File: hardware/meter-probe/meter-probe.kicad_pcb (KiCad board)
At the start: 4 copper layers, 40 x 74 mm, 40 parts, among them J1 Cable, J2 Cable, SW1 Sensor Button, U1 TSL2585, U2 M24C02-D, U3 PCA9527, U4 TC1301A-APA, U5 USBLC6-2SC6

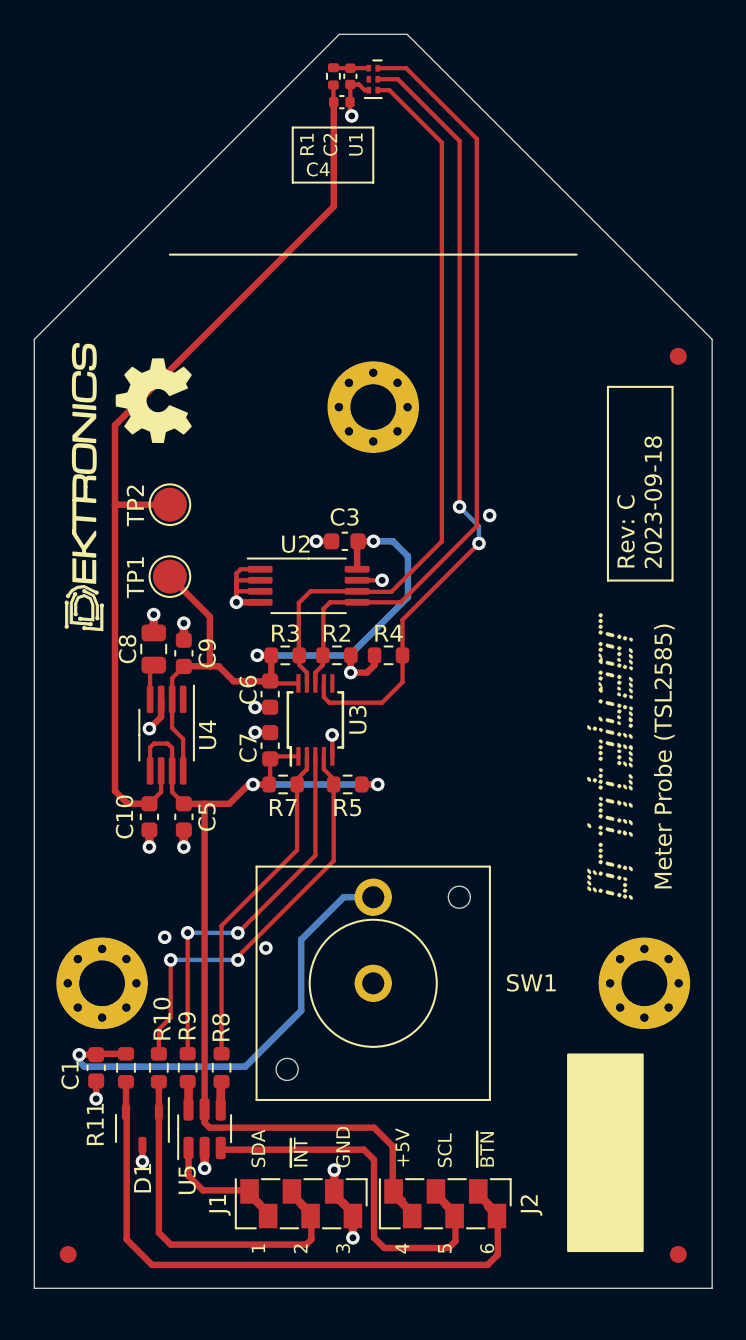
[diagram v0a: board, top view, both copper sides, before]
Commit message: Update meter probe with a variety of changes based on testing and eval
- Add a TCA9801 I2C buffer to remove the static offset induced by the
  PCA9527 and provide a clean 1.8V I2C signal to the sensor.
  While the board does work fine without this, the 0.5V static offset
  from the PCA9527 is too close for comfort to the sensor's 0.54V low
  level. So this is a proactive change to reduce potential issues later.
- Add a small series resistor to the push button, to limit the current
  across the debounce capacitor when the button is pressed.
- Add a series of test points at the board edge, so a pogo pin test clip
  can be used more easily to verify board operation prior to attachment
  of the interfae cable.
- Increase board length by 1mm to accomodate the test points.
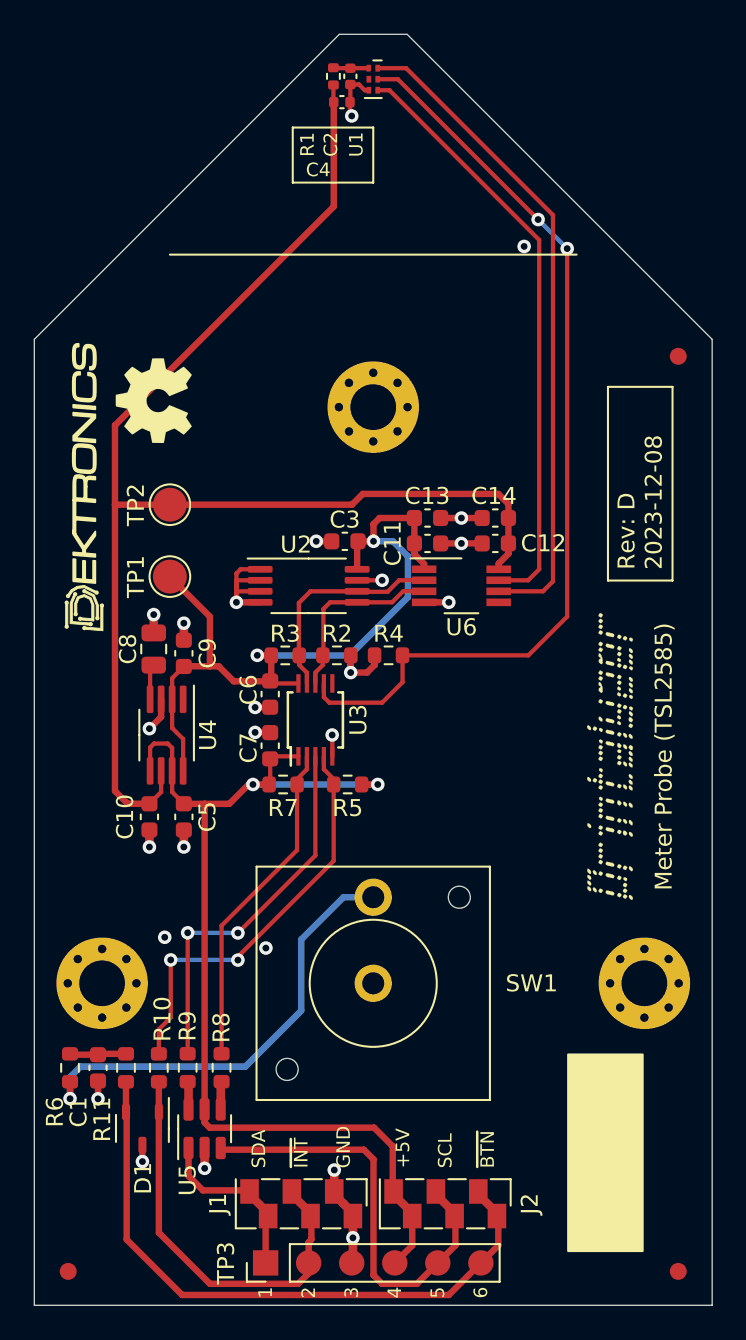
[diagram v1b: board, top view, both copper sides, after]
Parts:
- added C11: 0.1uF, Capacitor_SMD:C_0603_1608Metric, F.Cu at (123.2, 90.0)
- added C12: 0.1uF, Capacitor_SMD:C_0603_1608Metric, F.Cu at (127.2, 90.0)
- added C13: 1uF, Capacitor_SMD:C_0603_1608Metric, F.Cu at (123.2, 88.5)
- added C14: 1uF, Capacitor_SMD:C_0603_1608Metric, F.Cu at (127.2, 88.5)
- added R6: 220R, Resistor_SMD:R_0603_1608Metric, F.Cu at (102.1, 121.0)
- added TP3: Test, lib_fp:TestPoint_1x06_P2.54mm, F.Cu at (113.7, 132.5)
- added U6: TCA9801, Package_SO:VSSOP-8_3.0x3.0mm_P0.65mm, F.Cu at (125.2, 92.5)
- moved FID1 1.00 mm to (102.0, 133.0)
- moved FID2 1.00 mm to (138.0, 133.0)
- moved C1 0.11 mm to (103.8, 121.0)
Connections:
- R2 pad 2: /SENSOR_SDA -> /3V3_SDA
- R3 pad 2: /SENSOR_SCL -> /3V3_SCL
- SW1 pad 2: /PROBE_BTN -> Net-(R6-Pad1)
- U2 pad 5: /SENSOR_SDA -> /3V3_SDA
- U2 pad 6: /SENSOR_SCL -> /3V3_SCL
- U3 pad 8: /SENSOR_SDA -> /3V3_SDA
- U3 pad 9: /SENSOR_SCL -> /3V3_SCL
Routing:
- net Net-(R6-Pad1): track 0.00 -> 27.0 mm, vias 0 -> 1
- net +1V8: track 54.8 -> 79.4 mm
- net /PROBE_BTN: track 27.2 -> 3.20 mm, vias 1 -> 0
- net /3V3_SCL: track 0.00 -> 12.9 mm
- net /3V3_SDA: track 0.00 -> 11.0 mm
- net /SENSOR_INT: track 46.7 -> 55.4 mm
- net /SENSOR_SCL: track 43.5 -> 35.3 mm
- net GND: track 31.6 -> 39.4 mm, vias 20 -> 23
- net /SENSOR_SDA: track 46.1 -> 39.0 mm
- net +3.3V: track 44.1 -> 50.9 mm
- net +5V: track 57.4 -> 59.7 mm
- net /PROBE_CONN_SCL: track 21.5 -> 23.7 mm
- net /PROBE_CONN_INT: track 20.8 -> 22.8 mm
- net /PROBE_CONN_SDA: track 6.53 -> 8.14 mm
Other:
- board size 40 x 74 mm -> 40 x 75 mm

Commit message: Initial layout for USB meter probe design
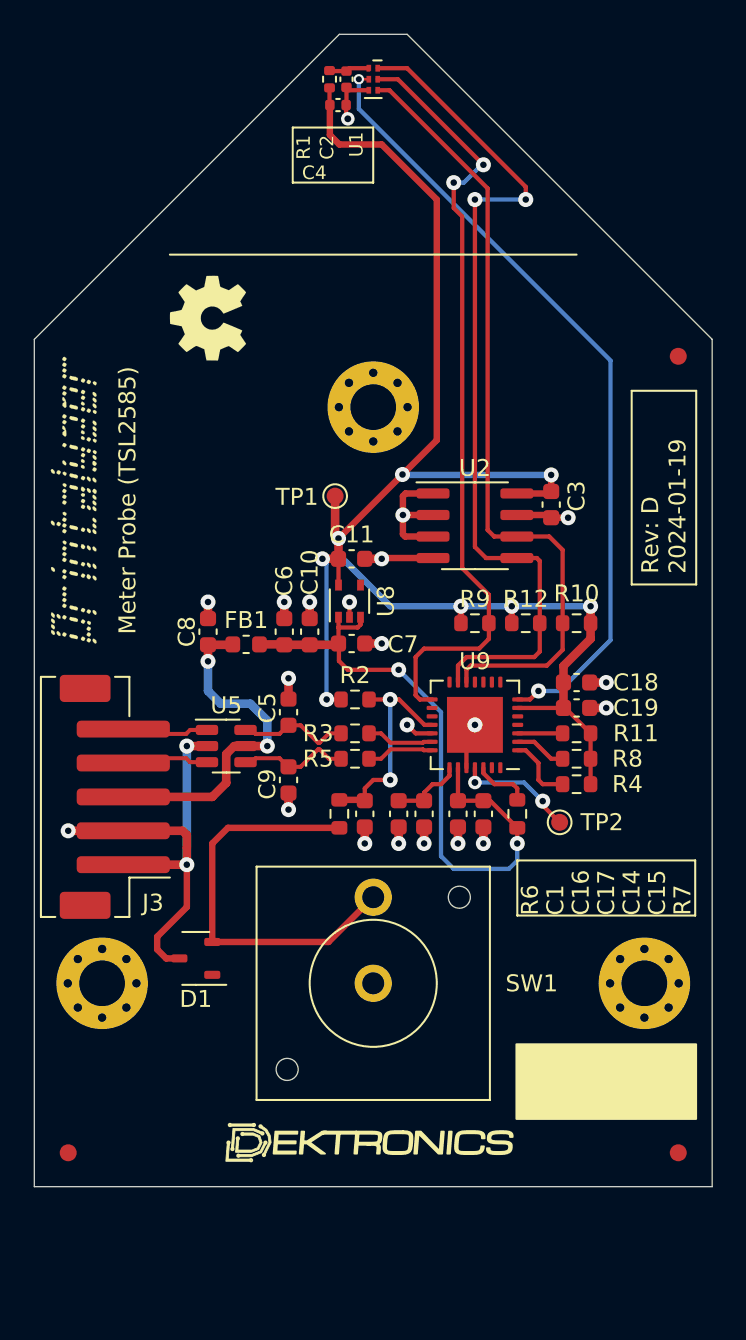
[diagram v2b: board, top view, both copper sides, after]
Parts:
- removed C12: 0.1uF, Capacitor_SMD:C_0603_1608Metric
- removed C13: 1uF, Capacitor_SMD:C_0603_1608Metric
- removed J1, J2: Cable, lib_fp:AVX_IDC-009175-003-001
- removed TP3: Test, lib_fp:TestPoint_1x06_P2.54mm
- removed U3: PCA9527, Package_SO:TSSOP-10_3x3mm_P0.5mm
- removed U4: TC1301A-APA, Package_SO:MSOP-8_3x3mm_P0.65mm
- removed U6: TCA9801, Package_SO:VSSOP-8_3.0x3.0mm_P0.65mm
- added C15: 0.1uF, Capacitor_SMD:C_0603_1608Metric, F.Cu at (126.5, 106.0)
- added C16: 4.7uF, Capacitor_SMD:C_0603_1608Metric, F.Cu at (121.5, 106.0)
- added C17: 0.1uF, Capacitor_SMD:C_0603_1608Metric, F.Cu at (123.0, 106.0)
- added C18: 4.7uF, Capacitor_SMD:C_0603_1608Metric, F.Cu at (132.0, 98.2)
- added C19: 0.1uF, Capacitor_SMD:C_0603_1608Metric, F.Cu at (132.0, 99.8)
- added FB1: 600R@100MHz, Inductor_SMD:L_0603_1608Metric, F.Cu at (112.5, 96.0)
- added J3: Cable, Connector_JST:JST_PH_B5B-PH-SM4-TB_1x05-1MP_P2.00mm_Vertical, F.Cu at (104.8, 105.0)
- added NT1: NetTie_2, NetTie:NetTie-2_SMD_Pad0.5mm, F.Cu at (109.0, 108.5)
- added R12: 1K, Resistor_SMD:R_0603_1608Metric, F.Cu at (129.0, 94.8)
- added U8: MIC5365-1.8YC5, Package_TO_SOT_SMD:SOT-353_SC-70-5, F.Cu at (118.6, 93.5)
- added U9: FT260Q, lib_fp:FTDI_WQFN-28-1EP_5x5mm_P0.5mm_EP3.3x3.3mm, F.Cu at (126.0, 100.8)
- C10: value 1uF -> 0.1uF
- C11, C7: value 0.1uF -> 1uF
- C14: value 1uF -> 4.7uF
- C5, C9: value 1uF -> 47pF
- C6: value 0.1uF -> 4.7uF
- C8: footprint Capacitor_SMD:C_0805_2012Metric -> Capacitor_SMD:C_0603_1608Metric
- R10: value 33R -> 1K
- R11: value 220R -> 10K
- R2: value 2K -> 10K
- R3: value 2K -> 33R
- R5: value 10K -> 33R
- R7: value 47K -> 5.1k
- R8, R9: value 33R -> 10K
- TP1: value 3.3V -> TestPoint; footprint TestPoint:TestPoint_Pad_D2.0mm -> TestPoint:TestPoint_Pad_D1.0mm
- TP2: value 1.8V -> TestPoint; footprint TestPoint:TestPoint_Pad_D2.0mm -> TestPoint:TestPoint_Pad_D1.0mm
- U2: value M24C02-D -> CAT24C08; footprint Package_SO:TSSOP-8_4.4x3mm_P0.65mm -> Package_SO:SOIC-8_3.9x4.9mm_P1.27mm
- moved LOGO 42.4 mm to (120.0, 125.2), turned to 0 degrees
- moved R10 36.0 mm to (132.0, 94.8), turned to 180 degrees
- moved G*** 35.1 mm to (102.3, 87.5)
- moved R11 33.1 mm to (132.0, 101.2), turned to 180 degrees
- moved R9 31.2 mm to (126.0, 94.8), turned to 0 degrees
- moved TP2 29.7 mm to (131.0, 106.5), turned to 180 degrees
- moved R8 27.8 mm to (132.0, 102.8), turned to 180 degrees
- moved U5 22.6 mm to (111.3, 102.0), turned to 0 degrees
- moved R6 21.8 mm to (118.0, 106.0)
- moved C1 21.7 mm to (119.5, 106.0)
- moved C14 17.6 mm to (125.0, 106.0), turned to -90 degrees
- moved C10 14.5 mm to (116.2, 95.2)
- moved R7 13.9 mm to (128.5, 106.0), turned to -90 degrees
- moved R4 13.5 mm to (132.0, 104.2), turned to 180 degrees
- moved C3 12.4 mm to (130.5, 87.8), turned to 90 degrees
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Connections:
- C10 pad 1: GND -> +5V
- C10 pad 2: +1V8 -> GND
- C11 pad 1: +3.3V -> +1V8
- C14 pad 1: +1V8 -> +5V
- C3 pad 2: +3.3V -> +1V8
- C5 pad 1: GND -> /USB_DI+
- C5 pad 2: +5V -> GND
- C6 pad 1: +3.3V -> +5V
- C7 pad 1: GND -> +5V
- C7 pad 2: +5V -> GND
- C8 pad 2: Net-(U4-BYPASS) -> VBUS
- C9 pad 1: GND -> /USB_DI-
- C9 pad 2: +3.3V -> GND
- D1 pad 1: /PROBE_CONN_INT -> unconnected-(D1-K-Pad1)
- D1 pad 2: /PROBE_CONN_BTN -> Net-(D1-K-Pad2)
- D1 pad 3: GND -> Earth
- R10 pad 1: /PROBE_INT -> +1V8
- R10 pad 2: /PROBE_CONN_INT -> /I2C_SCL
- R11 pad 1: /PROBE_BTN -> +1V8
- R11 pad 2: /PROBE_CONN_BTN -> Net-(U9-~{RESET})
- R2 pad 1: +3.3V -> +1V8
- R2 pad 2: /3V3_SDA -> /PROBE_BTN
- R3 pad 1: +3.3V -> /USB_D+
- R3 pad 2: /3V3_SCL -> /USB_DI+
- R4 pad 1: +3.3V -> +1V8
- R4 pad 2: /SENSOR_INT -> Net-(U9-DEBUGGER)
- R5 pad 1: +5V -> /USB_D-
- R5 pad 2: /PROBE_INT -> /USB_DI-
- R6 pad 1: Net-(R6-Pad1) -> Net-(D1-K-Pad2)
- R7 pad 1: +5V -> Net-(U9-VBUS_DET)
- R7 pad 2: /PROBE_SCL -> +5V
- R8 pad 1: /PROBE_SCL -> +1V8
- R8 pad 2: Net-(R8-Pad2) -> Net-(U9-~{STEST_RST})
- R9 pad 1: /PROBE_SDA -> +1V8
- R9 pad 2: Net-(R9-Pad2) -> /TSL_INT
- SW1 pad 2: Net-(R6-Pad1) -> Net-(D1-K-Pad2)
- TP1 pad 1: +3.3V -> +1V8
- TP2 pad 1: +1V8 -> Net-(U9-FSOURCE)
- U1 pad 2: unconnected-(U1-VSYNC/GPIO-Pad2) -> /TSL_VSYNC
- U1 pad 4: /SENSOR_SCL -> /I2C_SCL
- U1 pad 5: /SENSOR_INT -> /TSL_INT
- U1 pad 6: /SENSOR_SDA -> /I2C_SDA
- U2 pad 5: /3V3_SDA -> /I2C_SDA
- U2 pad 6: /3V3_SCL -> /I2C_SCL
- U2 pad 8: +3.3V -> +1V8
- U5 pad 1: /PROBE_CONN_SDA -> /USB_CONN_D+
- U5 pad 2: GND -> Earth
- U5 pad 3: /PROBE_CONN_SCL -> /USB_CONN_D-
- U5 pad 4: Net-(R8-Pad2) -> /USB_DI-
- U5 pad 5: +5V -> VBUS
- U5 pad 6: Net-(R9-Pad2) -> /USB_DI+
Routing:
- net /SENSOR_INT: track 55.4 -> 0.00 mm, vias 2 -> 0
- net /I2C_SDA: track 0.00 -> 51.5 mm, vias 0 -> 2
- net +3.3V: track 50.9 -> 0.00 mm, vias 3 -> 0
- net /TSL_VSYNC: track 0.00 -> 46.8 mm, vias 0 -> 2
- net /I2C_SCL: track 0.00 -> 46.7 mm
- net /TSL_INT: track 0.00 -> 46.4 mm, vias 0 -> 2
- net /SENSOR_SDA: track 39.0 -> 0.00 mm
- net /PROBE_CONN_BTN: track 35.7 -> 0.00 mm
- net /SENSOR_SCL: track 35.3 -> 0.00 mm
- net Net-(R6-Pad1): track 27.0 -> 0.00 mm, vias 1 -> 0
- net Net-(D1-K-Pad2): track 0.00 -> 24.3 mm
- net /PROBE_INT: track 24.0 -> 0.00 mm, vias 2 -> 0
- net /PROBE_CONN_SCL: track 23.7 -> 0.00 mm
- net /PROBE_CONN_INT: track 22.8 -> 0.00 mm
- net /PROBE_SDA: track 22.4 -> 0.00 mm, vias 2 -> 0
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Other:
- board size 40 x 75 mm -> 40 x 68 mm
- board text removed: "+5V"
- board text removed: "1"
- board text removed: "2"
- board text removed: "3"
- board text removed: "4"
- board text removed: "5"
- board text removed: "6"
- board text removed: "GND"
- board text removed: "SCL"
- board text removed: "SDA"
- board text removed: "~{BTN}"
- board text removed: "~{INT}"

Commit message: Clean up reference designators
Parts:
- renumbered C2 to C1, C14 to C10, C15 to C11, C16 to C12, C17 to C13, C18 to C14, C19 to C15, C3 to C16, C1 to C17, C4 to C2, C5 to C3, C9 to C4, C8 to C5, C10 to C7, C7 to C8, C11 to C9, J3 to J1, R7 to R10, R2 to R11, R6 to R12, R3 to R2, R5 to R3, R10 to R4, R12 to R5, R9 to R6, R11 to R7, R4 to R9, U5 to U2, U8 to U3, U9 to U4, U2 to U5

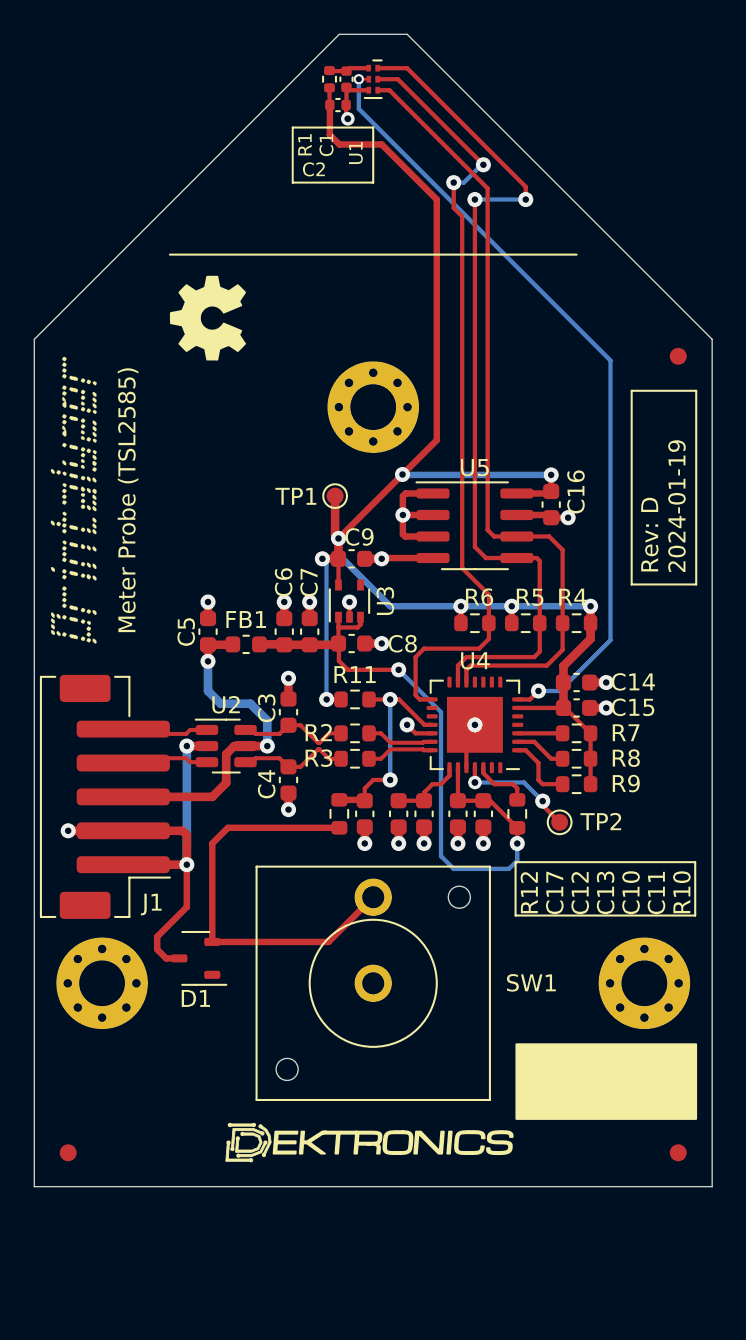
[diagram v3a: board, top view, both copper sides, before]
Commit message: Nudge some positions around
Moved the USB input components and routing to more closely match how the
evaluation board does it, only doing proper differential trace spacing
on the connector and FT260 endpoints.
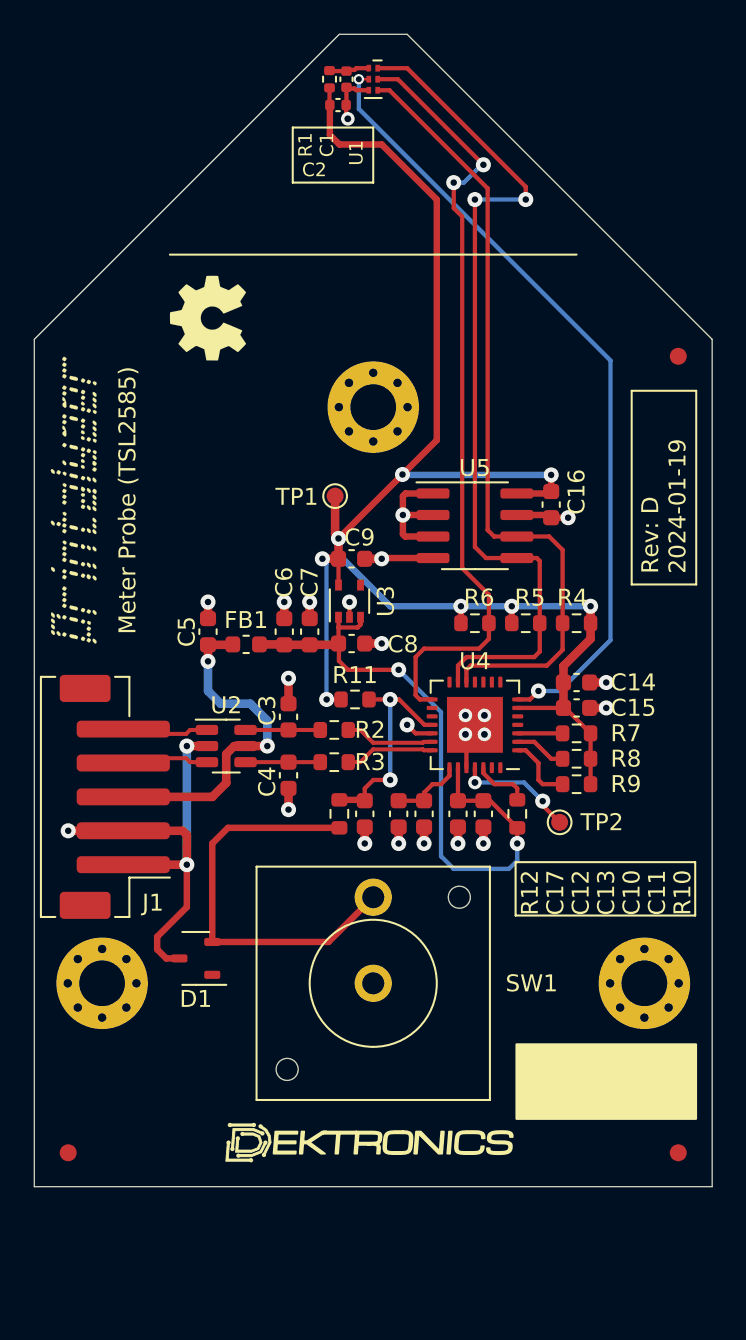
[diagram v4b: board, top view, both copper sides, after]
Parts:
- moved R2 1.24 mm to (117.7, 101.0)
- moved R3 1.24 mm to (117.7, 103.0)
- moved C3 0.28 mm to (115.0, 100.3)
- moved C4 0.28 mm to (115.0, 103.7)
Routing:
- net /USB_DI+: track 6.21 -> 4.41 mm
- net /USB_DI-: track 6.21 -> 4.41 mm
- net /USB_D-: track 3.98 -> 5.29 mm
- net /USB_D+: track 3.98 -> 5.29 mm
- net GND: vias 21 -> 24

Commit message: Meter probe changes from lab testing
Added pull-down resistor to DCD to prevent unwanted interrupts,
since it is enabled as part of enabling DI.

Added a series resistor and test point for the GPIOA pin that
is routed to VSYNC.

Various minor layout tweaks
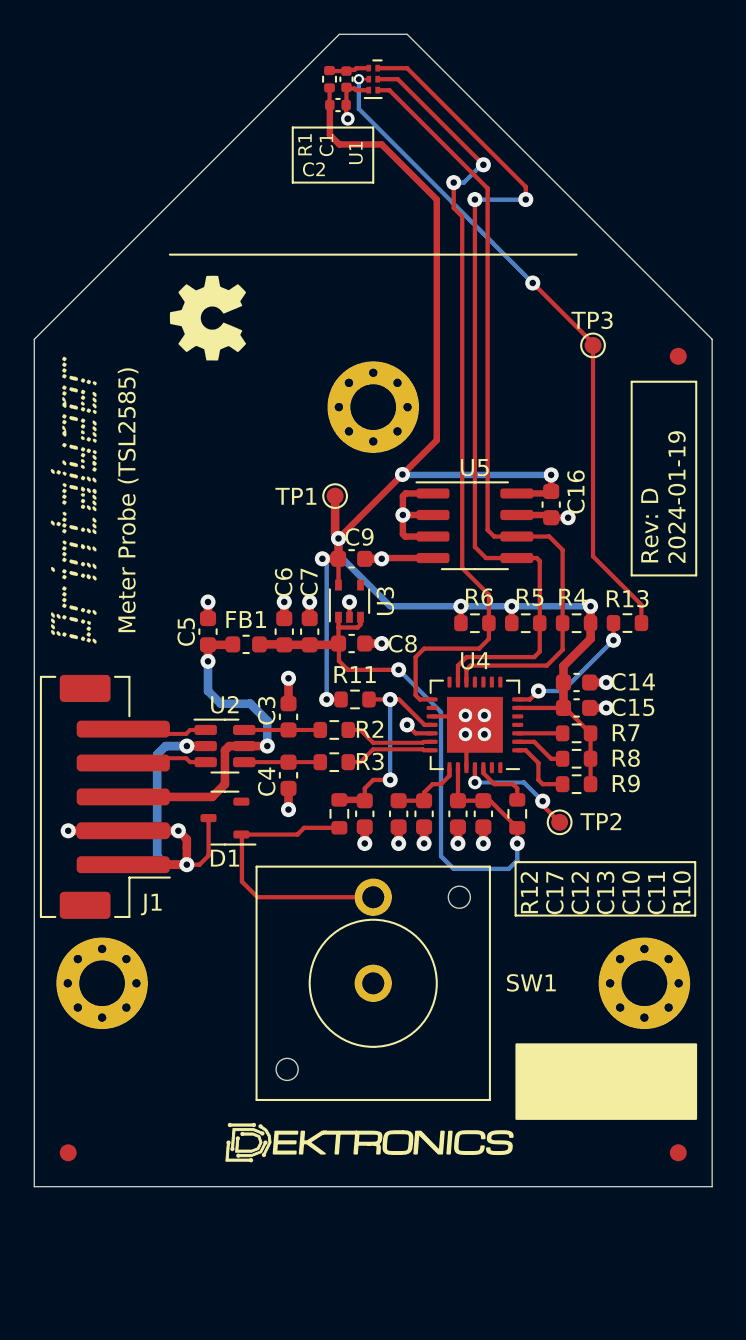
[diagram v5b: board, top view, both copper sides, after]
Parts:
- added R13: 33R, Resistor_SMD:R_0603_1608Metric, F.Cu at (135.0, 94.7)
- added TP3: TestPoint, TestPoint:TestPoint_Pad_D1.0mm, F.Cu at (133.0, 78.4)
- moved D1 8.46 mm to (111.2, 106.2)
- moved U2 0.08 mm to (111.2, 102.0)
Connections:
- D1 pad 1: unconnected-(D1-K-Pad1) -> Net-(D1-K-Pad1)
- D1 pad 2: Net-(D1-K-Pad2) -> unconnected-(D1-K-Pad2)
- R12 pad 1: Net-(D1-K-Pad2) -> Net-(D1-K-Pad1)
- SW1 pad 2: Net-(D1-K-Pad2) -> Net-(D1-K-Pad1)
- U4 pad 17: unconnected-(U4-DIO10-Pad17) -> GND
- U4 pad 7: /TSL_VSYNC -> Net-(U4-DIO0)
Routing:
- net Net-(D1-K-Pad2): track 24.3 -> 0.00 mm
- net Net-(D1-K-Pad1): track 0.00 -> 16.8 mm
- net Net-(U4-DIO0): track 0.00 -> 8.11 mm, vias 0 -> 2
- net /TSL_VSYNC: track 46.8 -> 39.6 mm
- net GND: track 43.0 -> 44.8 mm, vias 24 -> 25
- net Earth: track 19.2 -> 18.6 mm
